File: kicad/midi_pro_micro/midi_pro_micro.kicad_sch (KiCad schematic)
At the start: 23 parts, among them J1 DIN-5_180degree, J2 DIN-5_180degree, J3 Conn_01x12, J4 Conn_01x16_Pin, J6 Conn_01x04, U1 ProMicro, U2 AT25xxx, U3 6N138

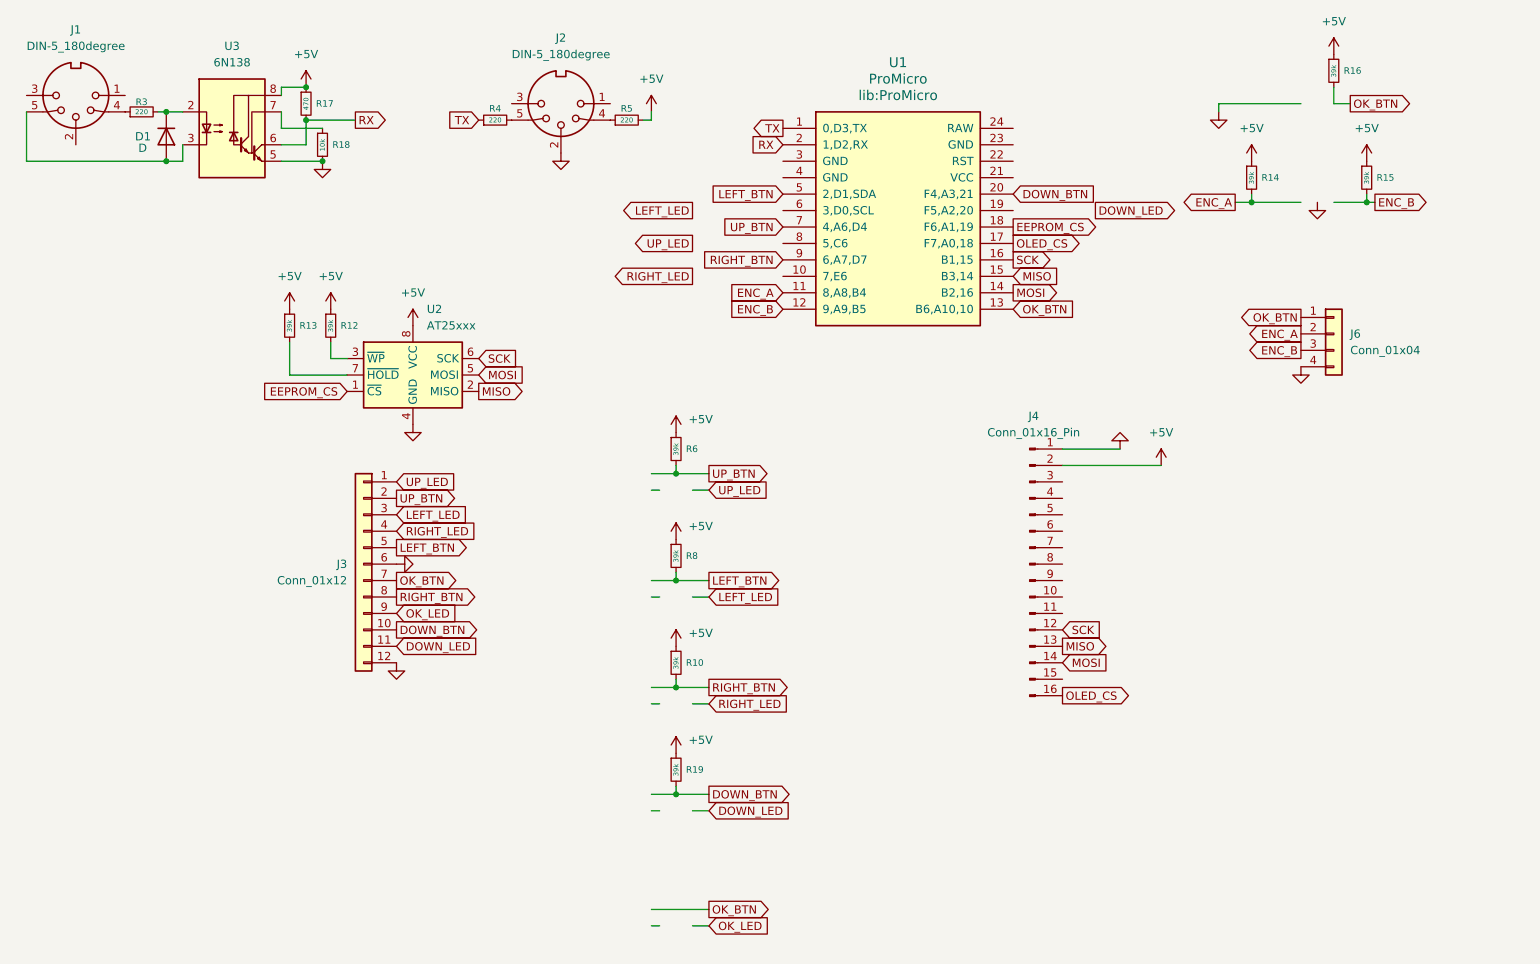
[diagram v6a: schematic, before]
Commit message: Add 2.42 OLED display
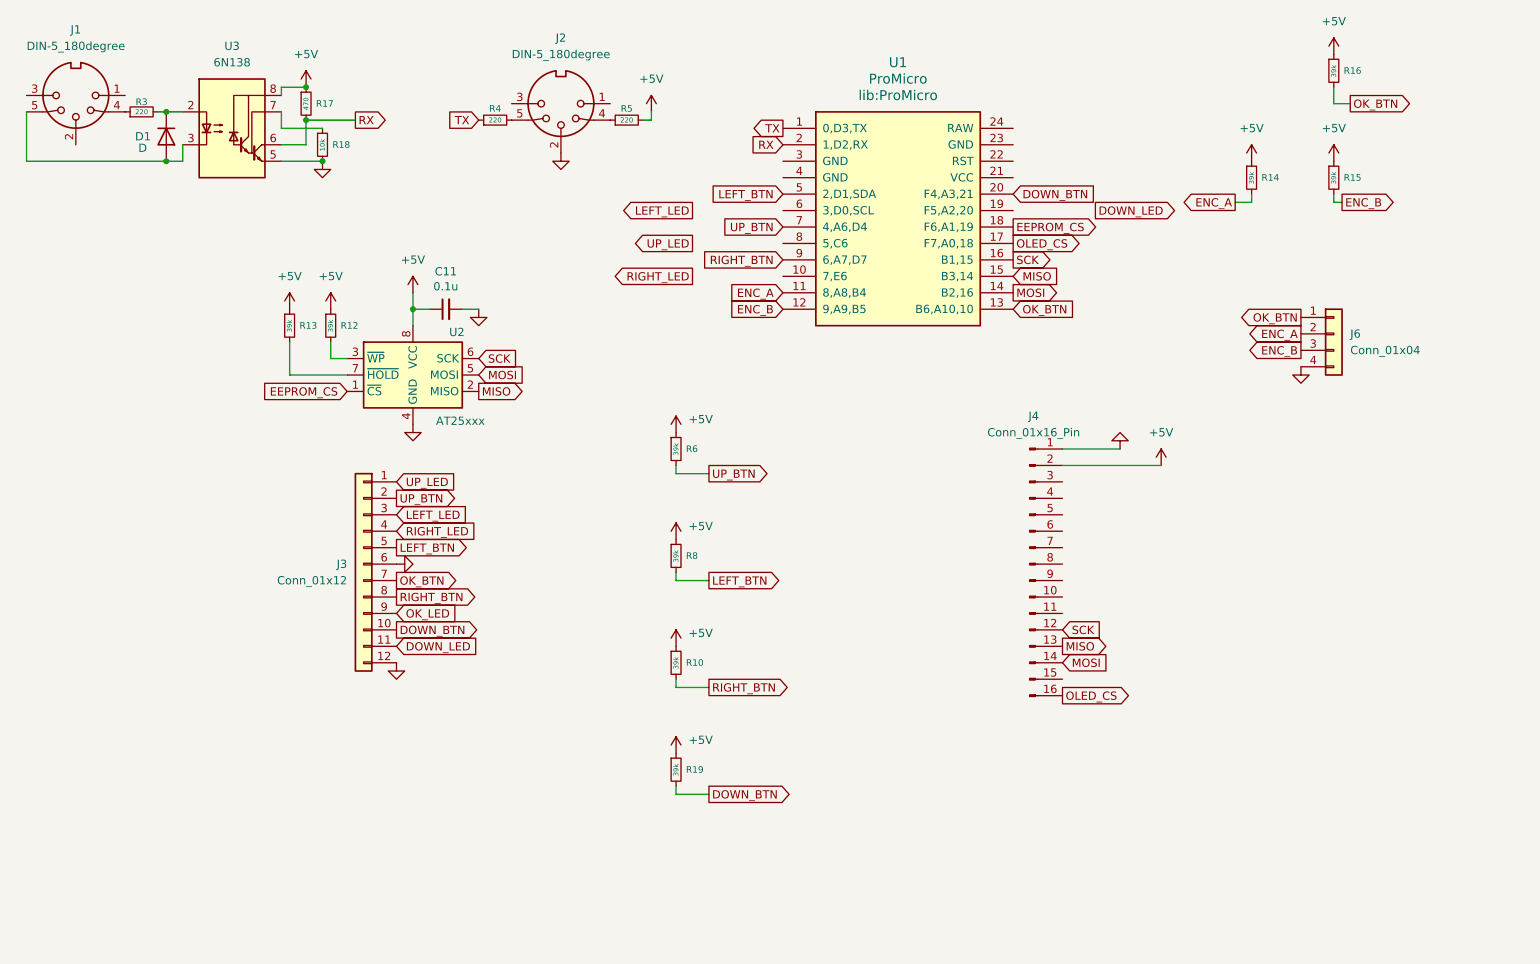
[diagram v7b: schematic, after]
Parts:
- added C11: 0.1u, Capacitor_SMD:C_0805_2012Metric, symbol Device:C_Small
- U2: footprint (none) -> Package_SO:SO-8_3.9x4.9mm_P1.27mm
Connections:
- net +5V: now also C11.1
- net GND: now also C11.2
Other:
- moved on the sheet: R15

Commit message: Add case body prototype
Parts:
- added H1, H2, H3, H4: MountingHole, MountingHole:MountingHole_3.2mm_M3_DIN965, symbol Mechanical:MountingHole
